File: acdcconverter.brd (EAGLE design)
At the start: 70.2 x 30.5 mm, 21 parts

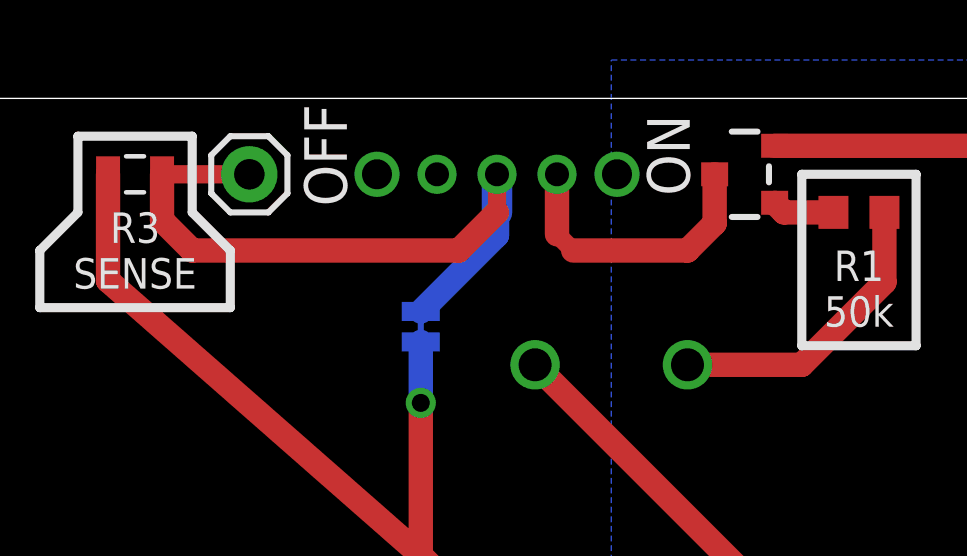
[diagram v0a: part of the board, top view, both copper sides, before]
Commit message: Fixed mosfet switch circuit
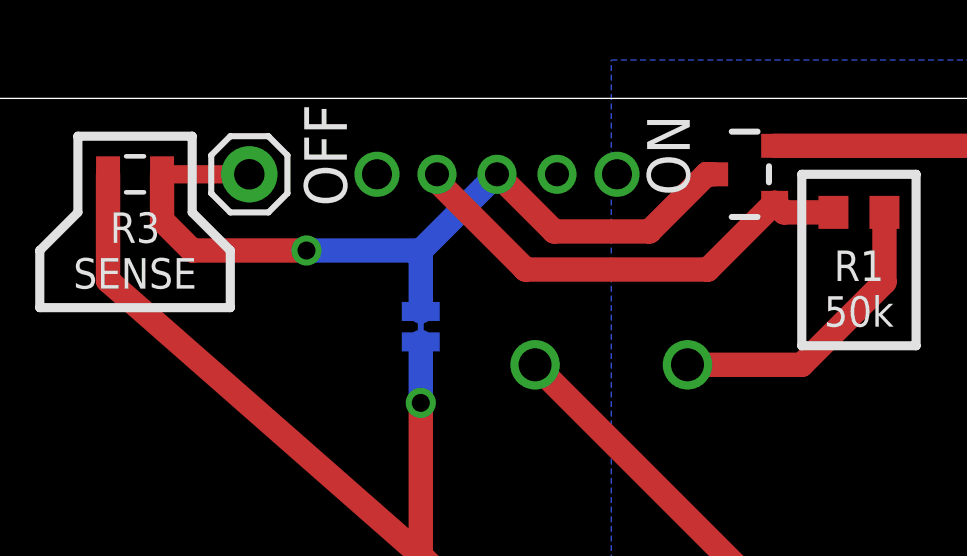
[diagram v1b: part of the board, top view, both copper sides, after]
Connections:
- removed net N$5: U$4.2, U$5.NO
- net N$3: now also U$5.NC
- net N$4: now also U$4.2
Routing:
- net N$3: track 2.09 -> 15.7 mm
- net N$5: track 9.49 -> 0.00 mm
- net N$4: track 24.7 -> 27.9 mm, vias 0 -> 1
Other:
- board text added: "REV 0.1 MAR/20/2016"
- board text removed: "REV 0 MAR/20/2016"
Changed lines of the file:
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@@
 <text x="14.605" y="30.48" size="1.016" layer="21" font="vector" ratio="16" align="center">AC-DC CONVERTER</text>
 <text x="14.605" y="29.21" size="1.016" layer="21" font="vector" ratio="16" align="center">HARRISON JONES</text>
-<text x="6.35" y="17.145" size="1.016" layer="22" font="vector" ratio="16" rot="MR270" align="center">REV 0 MAR/20/2016</text>
+<text x="6.35" y="17.145" size="1.016" layer="22" font="vector" ratio="16" rot="MR270" align="center">REV 0.1 MAR/20/2016</text>
 <text x="14.605" y="27.94" size="1.016" layer="21" font="vector" ratio="16" align="center">HHJ.ME</text>
 <circle x="15.24" y="5.08" radius="1.419903125" width="0.4064" layer="22"/>
@@
 <wire x1="48.625" y1="28.26" x2="48.94" y2="27.94" width="0.8128" layer="1"/>
 <wire x1="48.94" y1="27.94" x2="50.585" y2="27.94" width="0.8128" layer="1"/>
+<contactref element="U$5" pad="NC"/>
+<wire x1="37.37" y1="29.21" x2="37.37" y2="28.9875" width="0.8128" layer="1"/>
+<wire x1="37.37" y1="28.9875" x2="40.3225" y2="26.035" width="0.8128" layer="1"/>
+<wire x1="40.3225" y1="26.035" x2="46.4" y2="26.035" width="0.8128" layer="1"/>
+<wire x1="46.4" y1="26.035" x2="48.625" y2="28.26" width="0.8128" layer="1"/>
 </signal>
 <signal name="VCCIO">
@@
 <contactref element="R3" pad="1"/>
 <contactref element="SJ1" pad="1"/>
-<contactref element="U$5" pad="C"/>
 <contactref element="JP2" pad="1"/>
 <wire x1="28.205" y1="29.21" x2="28.205" y2="27.675" width="0.8128" layer="1"/>
 <wire x1="28.205" y1="27.675" x2="29.21" y2="26.67" width="0.8128" layer="1"/>
-<wire x1="29.21" y1="26.67" x2="38.1" y2="26.67" width="0.8128" layer="1"/>
-<wire x1="38.1" y1="26.67" x2="39.37" y2="27.94" width="0.8128" layer="1"/>
-<wire x1="39.37" y1="27.94" x2="39.37" y2="29.21" width="0.6096" layer="1"/>
 <wire x1="28.205" y1="29.21" x2="31.115" y2="29.21" width="0.6096" layer="1"/>
-<wire x1="39.37" y1="27.94" x2="39.37" y2="29.21" width="1.016" layer="16"/>
-<wire x1="36.83" y1="24.638" x2="39.37" y2="27.178" width="0.8128" layer="16"/>
-<wire x1="39.37" y1="27.178" x2="39.37" y2="29.21" width="0.8128" layer="16"/>
-</signal>
-<signal name="N$5">
-<contactref element="U$5" pad="NO"/>
 <contactref element="U$4" pad="2"/>
-<wire x1="41.37" y1="29.21" x2="41.37" y2="27.21" width="0.8128" layer="1"/>
-<wire x1="41.37" y1="27.21" x2="41.91" y2="26.67" width="0.6096" layer="1"/>
-<wire x1="41.91" y1="26.67" x2="45.72" y2="26.67" width="0.8128" layer="1"/>
-<wire x1="45.72" y1="26.67" x2="46.625" y2="27.575" width="0.8128" layer="1"/>
-<wire x1="46.625" y1="27.575" x2="46.625" y2="29.21" width="0.8128" layer="1"/>
+<contactref element="U$5" pad="C"/>
+<wire x1="46.625" y1="29.21" x2="46.355" y2="29.21" width="0.8128" layer="1"/>
+<wire x1="46.355" y1="29.21" x2="44.45" y2="27.305" width="0.8128" layer="1"/>
+<wire x1="44.45" y1="27.305" x2="41.275" y2="27.305" width="0.8128" layer="1"/>
+<wire x1="41.275" y1="27.305" x2="39.37" y2="29.21" width="0.8128" layer="1"/>
+<wire x1="36.83" y1="24.638" x2="36.83" y2="26.67" width="0.8128" layer="16"/>
+<wire x1="36.83" y1="26.67" x2="39.37" y2="29.21" width="0.8128" layer="16"/>
+<wire x1="29.21" y1="26.67" x2="33.02" y2="26.67" width="0.8128" layer="1"/>
+<via x="33.02" y="26.67" extent="1-16" drill="0.6" shape="square"/>
+<wire x1="33.02" y1="26.67" x2="36.83" y2="26.67" width="0.8128" layer="16"/>
 </signal>
 </signals>

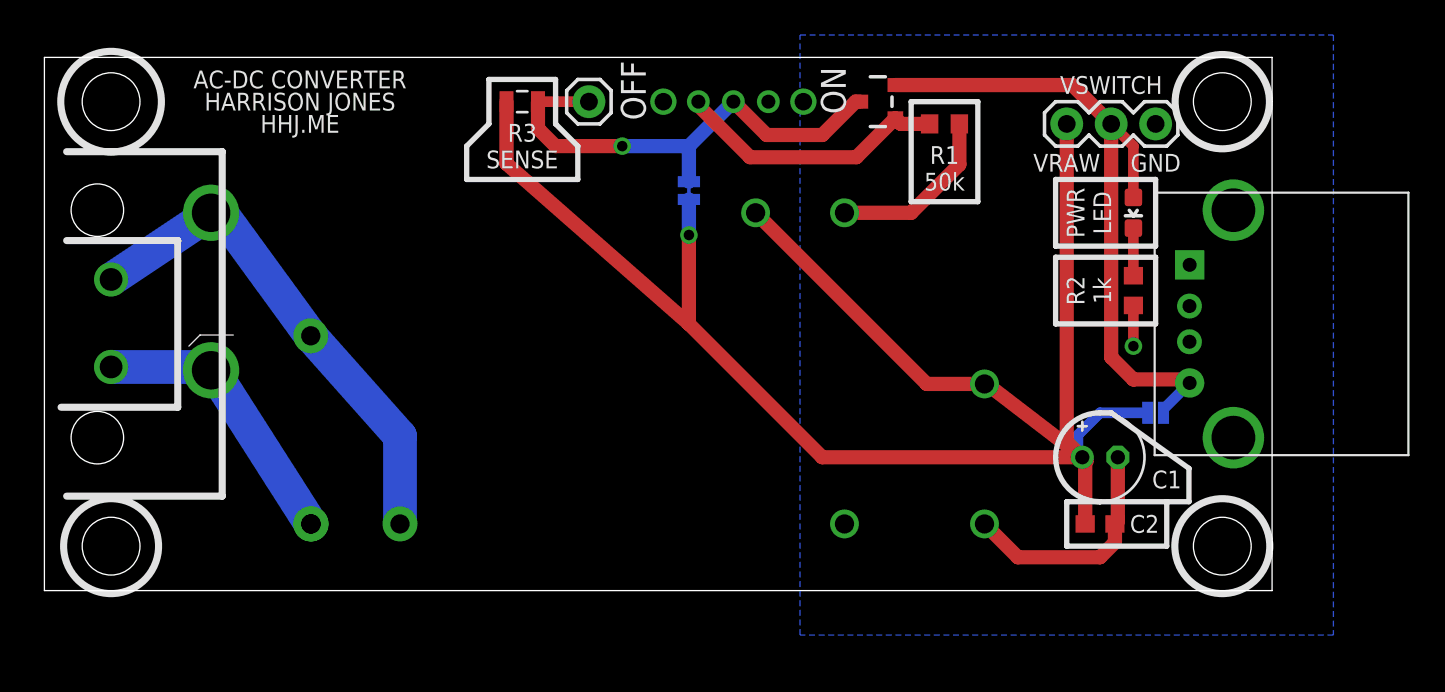
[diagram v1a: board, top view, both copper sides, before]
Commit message: Updated MOSFET again
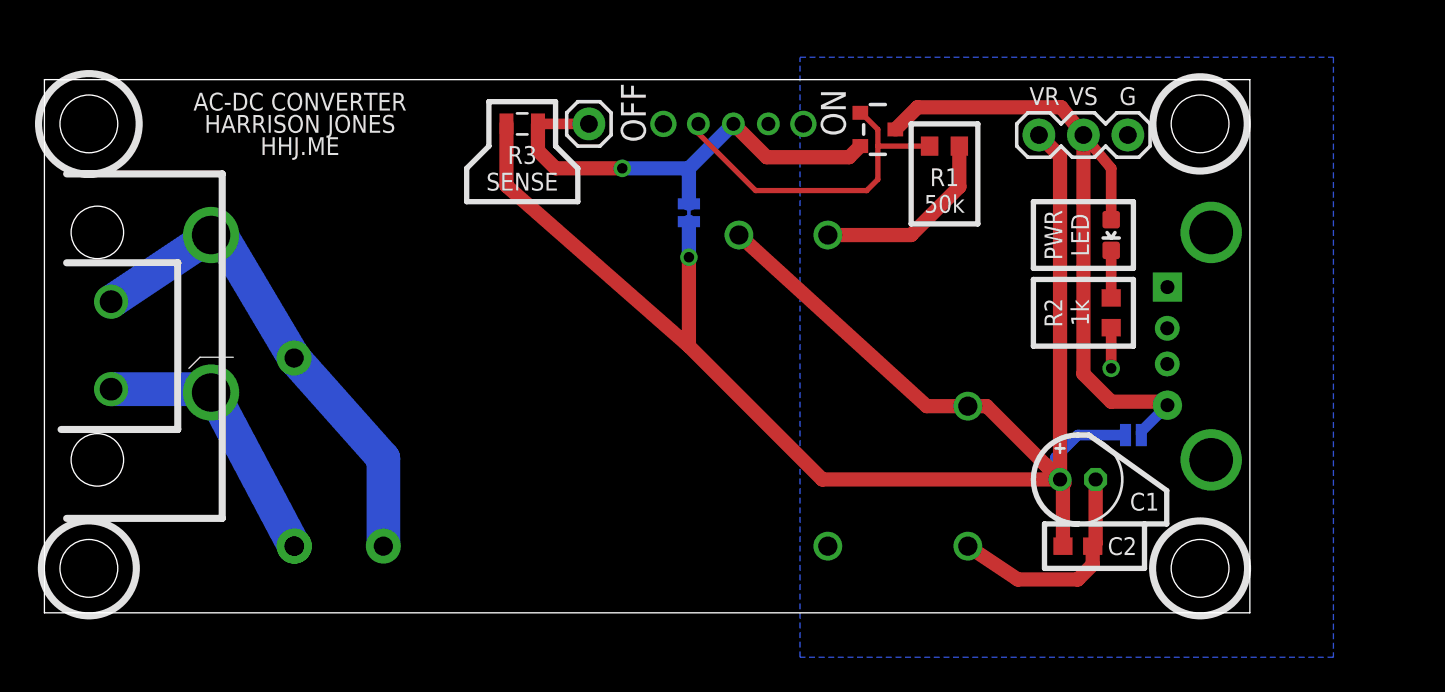
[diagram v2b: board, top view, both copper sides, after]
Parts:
- removed U$4: DMG2305UXDMG2305UX, HHJ:SOT23-3
- added U$8: MOSFET-PDMG2305UX, HHJ:SOT23-3
- moved C1 1.80 mm to (59.1, 7.62)
- moved C2 1.80 mm to (59.1, 3.81)
- moved SJ2 1.80 mm to (62.2, 10.2)
- moved STANDOFF2 1.80 mm to (2.54, 2.54)
- moved STANDOFF1 1.80 mm to (2.54, 27.9)
- moved U$7 1.80 mm to (66.7, 15.2)
- moved STANDOFF3 1.80 mm to (66.0, 2.54)
- moved PWR 1.80 mm to (61.0, 21.6)
- moved R2 1.80 mm to (61.0, 17.1)
- moved STANDOFF4 1.80 mm to (66.0, 27.9)
- moved JP4 1.71 mm to (61.9, 27.3)
- moved U$2 1.59 mm to (44.8, 3.81)
- moved U$3 1.59 mm to (52.8, 3.81)
- moved U$1 1.27 mm to (9.53, 15.2)
- moved JP2 1.27 mm to (31.1, 27.9)
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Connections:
- net N$3: now also U$8.3; no longer U$4.3
- net N$4: now also U$8.1; no longer U$4.2
- net VCCIO: now also U$8.2; no longer U$4.1
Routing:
- net N$3: track 15.7 -> 19.6 mm
- net VCC: track 103.5 -> 104.2 mm
- net N$4: track 27.9 -> 27.4 mm
- net AC/N: track 28.8 -> 28.3 mm
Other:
- board size 70.2 x 30.5 mm -> 68.9 x 30.5 mm
- board text added: "G"
- board text added: "VR"
- board text added: "VS"

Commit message: Rounded the corners
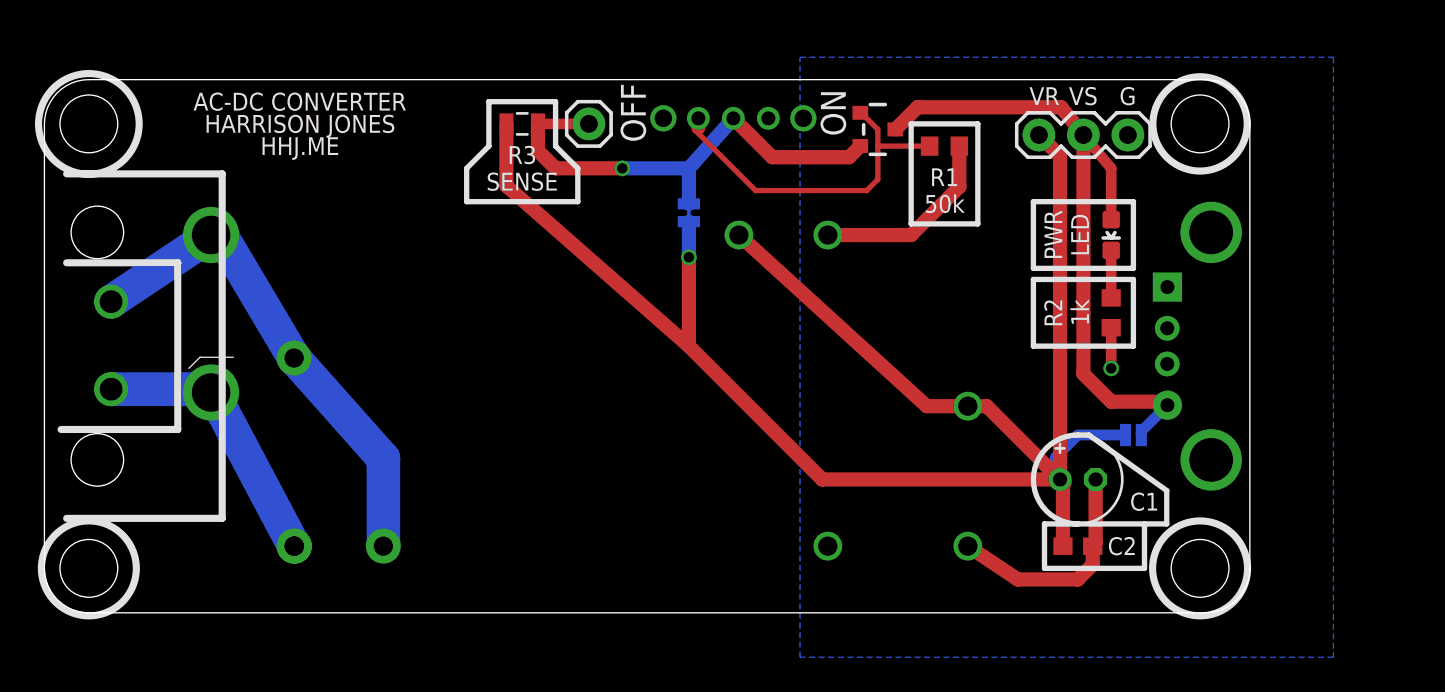
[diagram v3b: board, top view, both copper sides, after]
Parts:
- moved U$5 0.32 mm to (39.4, 28.3)
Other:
- outline, holes or cut-outs redrawn
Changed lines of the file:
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@@
 <board>
 <plain>
-<wire x1="0" y1="0" x2="68.885" y2="0" width="0" layer="20"/>
-<wire x1="68.885" y1="0" x2="68.885" y2="30.47" width="0" layer="20"/>
-<wire x1="68.885" y1="30.47" x2="0" y2="30.47" width="0" layer="20"/>
-<wire x1="0" y1="30.47" x2="0" y2="0" width="0" layer="20"/>
+<wire x1="0" y1="27.93" x2="0" y2="2.54" width="0" layer="20"/>
+<wire x1="0" y1="2.54" x2="2.54" y2="0" width="0" layer="20" curve="90"/>
+<wire x1="2.54" y1="0" x2="66.345" y2="0" width="0" layer="20"/>
+<wire x1="66.345" y1="0" x2="68.885" y2="2.54" width="0" layer="20" curve="90"/>
+<wire x1="68.885" y1="2.54" x2="68.885" y2="27.93" width="0" layer="20"/>
+<wire x1="68.885" y1="27.93" x2="66.345" y2="30.47" width="0" layer="20" curve="90"/>
+<wire x1="66.345" y1="30.47" x2="2.54" y2="30.47" width="0" layer="20"/>
+<wire x1="2.54" y1="30.47" x2="0" y2="27.93" width="0" layer="20" curve="90"/>
 <text x="21.9075" y="16.51" size="1.27" layer="22" font="vector" ratio="16" rot="MR90" align="center">DANGER HIGH VOLTAGE</text>
 <text x="24.4475" y="15.875" size="1.27" layer="22" font="vector" ratio="16" rot="MR90" align="center">LOW VOLTAGE</text>
@@
 </class>
 </classes>
-<designrules name="default">
+<designrules name="SeeedStudio_2layer_DRU_no_angle_20140221">
 <description language="de">&lt;b&gt;EAGLE Design Rules&lt;/b&gt;
 &lt;p&gt;
@@
 necessary adjustments and save your customized
 design rules under a new name.</description>
+<description language="zh">&lt;b&gt;Seeed Studio EAGLE Design Rules&lt;/b&gt;
+</description>
 <param name="layerSetup" value="(1*16)"/>
-<param name="mtCopper" value="0.035mm 0.035mm 0.035mm 0.035mm 0.035mm 0.035mm 0.035mm 0.035mm 0.035mm 0.035mm 0.035mm 0.035mm 0.035mm 0.035mm 0.035mm 0.035mm"/>
-<param name="mtIsolate" value="1.5mm 0.15mm 0.2mm 0.15mm 0.2mm 0.15mm 0.2mm 0.15mm 0.2mm 0.15mm 0.2mm 0.15mm 0.2mm 0.15mm 0.2mm"/>
-<param name="mdWireWire" value="8mil"/>
-<param name="mdWirePad" value="8mil"/>
-<param name="mdWireVia" value="8mil"/>
-<param name="mdPadPad" value="8mil"/>
-<param name="mdPadVia" value="8mil"/>
-<param name="mdViaVia" value="8mil"/>
-<param name="mdSmdPad" value="8mil"/>
-<param name="mdSmdVia" value="8mil"/>
-<param name="mdSmdSmd" value="8mil"/>
+<param name="mtCopper" value="0.035mm 0.0175mm 0.035mm 0.035mm 0.035mm 0.035mm 0.035mm 0.035mm 0.035mm 0.035mm 0.035mm 0.035mm 0.035mm 0.035mm 0.0175mm 0.035mm"/>
+<param name="mtIsolate" value="1.5mm 1.1mm 0.2mm 0.15mm 0.2mm 0.15mm 0.2mm 0.15mm 0.2mm 0.15mm 0.2mm 0.15mm 0.2mm 0.15mm 0.2mm"/>
+<param name="mdWireWire" value="6mil"/>
+<param name="mdWirePad" value="6mil"/>
+<param name="mdWireVia" value="6mil"/>
+<param name="mdPadPad" value="6mil"/>
+<param name="mdPadVia" value="6mil"/>
+<param name="mdViaVia" value="6mil"/>
+<param name="mdSmdPad" value="0mil"/>
+<param name="mdSmdVia" value="0mil"/>
+<param name="mdSmdSmd" value="0mil"/>
 <param name="mdViaViaSameLayer" value="8mil"/>
 <param name="mnLayersViaInSmd" value="2"/>
-<param name="mdCopperDimension" value="40mil"/>
-<param name="mdDrill" value="8mil"/>
+<param name="mdCopperDimension" value="10mil"/>
+<param name="mdDrill" value="10mil"/>
 <param name="mdSmdStop" value="0mil"/>
-<param name="msWidth" value="10mil"/>
-<param name="msDrill" value="24mil"/>
-<param name="msMicroVia" value="9.99mm"/>
+<param name="msWidth" value="6mil"/>
+<param name="msDrill" value="12mil"/>
+<param name="msMicroVia" value="12mil"/>
 <param name="msBlindViaRatio" value="0.5"/>
 <param name="rvPadTop" value="0.25"/>
@@
 <param name="rlMinPadBottom" value="10mil"/>
 <param name="rlMaxPadBottom" value="20mil"/>
-<param name="rlMinViaOuter" value="8mil"/>
+<param name="rlMinViaOuter" value="6mil"/>
 <param name="rlMaxViaOuter" value="20mil"/>
-<param name="rlMinViaInner" value="8mil"/>
+<param name="rlMinViaInner" value="6mil"/>
 <param name="rlMaxViaInner" value="20mil"/>
 <param name="rlMinMicroViaOuter" value="4mil"/>
@@
 <param name="psTop" value="-1"/>
 <param name="psBottom" value="-1"/>
-<param name="psFirst" value="-1"/>
+<param name="psFirst" value="0"/>
 <param name="psElongationLong" value="100"/>
 <param name="psElongationOffset" value="100"/>
 <param name="mvStopFrame" value="1"/>
 <param name="mvCreamFrame" value="0"/>
-<param name="mlMinStopFrame" value="4mil"/>
-<param name="mlMaxStopFrame" value="4mil"/>
+<param name="mlMinStopFrame" value="2mil"/>
+<param name="mlMaxStopFrame" value="2mil"/>
 <param name="mlMinCreamFrame" value="0mil"/>
 <param name="mlMaxCreamFrame" value="0mil"/>
-<param name="mlViaStopLimit" value="0mil"/>
+<param name="mlViaStopLimit" value="100mil"/>
 <param name="srRoundness" value="0"/>
 <param name="srMinRoundness" value="0mil"/>
@@
 <param name="checkAngle" value="0"/>
 <param name="checkFont" value="1"/>
-<param name="checkRestrict" value="1"/>
+<param name="checkRestrict" value="0"/>
 <param name="useDiameter" value="13"/>
 <param name="maxErrors" value="50"/>
@@
 <attribute name="VALUE" x="38.481" y="23.8125" size="0.4064" layer="28" rot="MR270"/>
 </element>
-<element name="U$5" library="HHJ" package="SWITCH-1825232-1" value="SWITCH-SPDT" x="39.37" y="27.94" smashed="yes" rot="R180"/>
+<element name="U$5" library="HHJ" package="SWITCH-1825232-1" value="SWITCH-SPDT" x="39.37" y="28.2575" smashed="yes" rot="R180"/>
 <element name="STANDOFF1" library="SparkFun-Electromechanical" package="STAND-OFF" value="STAND-OFF" x="2.54" y="27.94"/>
 <element name="STANDOFF2" library="SparkFun-Electromechanical" package="STAND-OFF" value="STAND-OFF" x="2.54" y="2.54"/>
@@
 <contactref element="R1" pad="2"/>
 <contactref element="U$5" pad="NC"/>
-<wire x1="37.37" y1="27.94" x2="37.37" y2="27.7175" width="0.8128" layer="1"/>
+<wire x1="37.37" y1="28.2575" x2="37.37" y2="27.7175" width="0.8128" layer="1"/>
 <contactref element="U$8" pad="3"/>
 <wire x1="46.625" y1="28.5725" x2="46.675" y2="28.5725" width="0.3048" layer="1"/>
@@
 <wire x1="28.205" y1="27.94" x2="31.115" y2="27.94" width="0.6096" layer="1"/>
 <contactref element="U$5" pad="C"/>
-<wire x1="45.9875" y1="26.035" x2="41.275" y2="26.035" width="0.8128" layer="1"/>
-<wire x1="41.275" y1="26.035" x2="39.37" y2="27.94" width="0.8128" layer="1"/>
+<wire x1="45.9875" y1="26.035" x2="41.5925" y2="26.035" width="0.8128" layer="1"/>
+<wire x1="41.5925" y1="26.035" x2="39.37" y2="28.2575" width="0.8128" layer="1"/>
 <wire x1="36.83" y1="23.368" x2="36.83" y2="25.4" width="0.8128" layer="16"/>
-<wire x1="36.83" y1="25.4" x2="39.37" y2="27.94" width="0.8128" layer="16"/>
+<wire x1="36.83" y1="25.4" x2="39.37" y2="28.2575" width="0.8128" layer="16"/>
 <wire x1="29.21" y1="25.4" x2="33.02" y2="25.4" width="0.8128" layer="1"/>
 <via x="33.02" y="25.4" extent="1-16" drill="0.6" shape="square"/>
